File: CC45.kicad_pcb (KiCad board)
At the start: 2 copper layers, 247 x 80.8 mm, 122 parts, among them J1 AVR-ISP-6, SW1 RESET, SW10 K08, SW11 K09, SW12 K0A, SW13 K0B, SW14 K0C, SW15 K10, SW16 K11, SW17 K12, SW18 K13, SW19 K14, SW2 K00, SW20 K15, SW21 K16, SW22 K17, SW23 K18, SW24 K19, SW25 K1A, SW26 K1B, SW27 K20, SW28 K21, SW29 K22, SW3 K01, SW30 K23, SW31 K24, SW32 K25, SW33 K26, SW34 K27, SW35 K28, SW36 K29, SW37 K2A, SW38 K2B, SW39 K30, SW4 K02, SW40 K31, SW41 K32, SW42 K33, SW43 K34, SW44 K36, SW45 K38, SW46 K39, SW47 K3A, SW48 K3B, SW5 K03, SW6 K04, SW7 K05, SW8 K06, SW9 K07, U1 ATmega32U4-AU, U2 PRTR5V0U2X, X1 XTAL

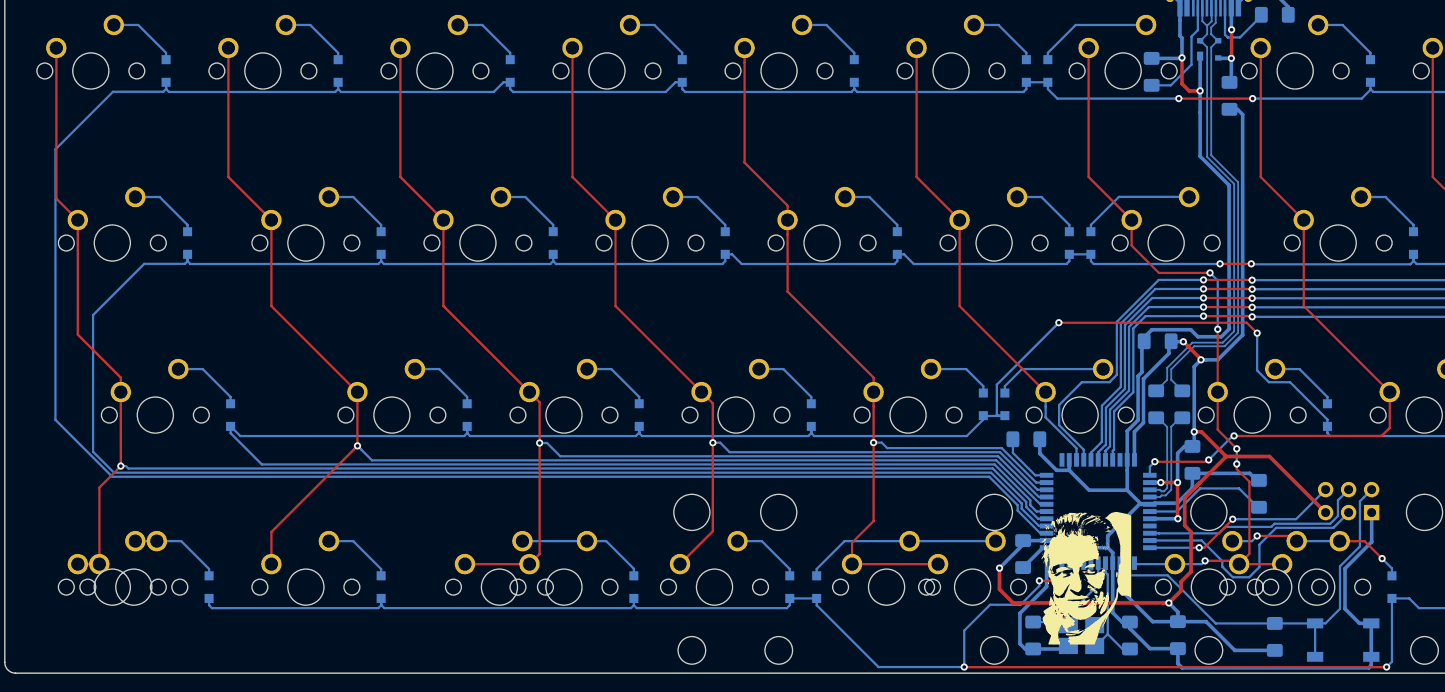
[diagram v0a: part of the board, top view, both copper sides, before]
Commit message: Add a decoupling capacitor
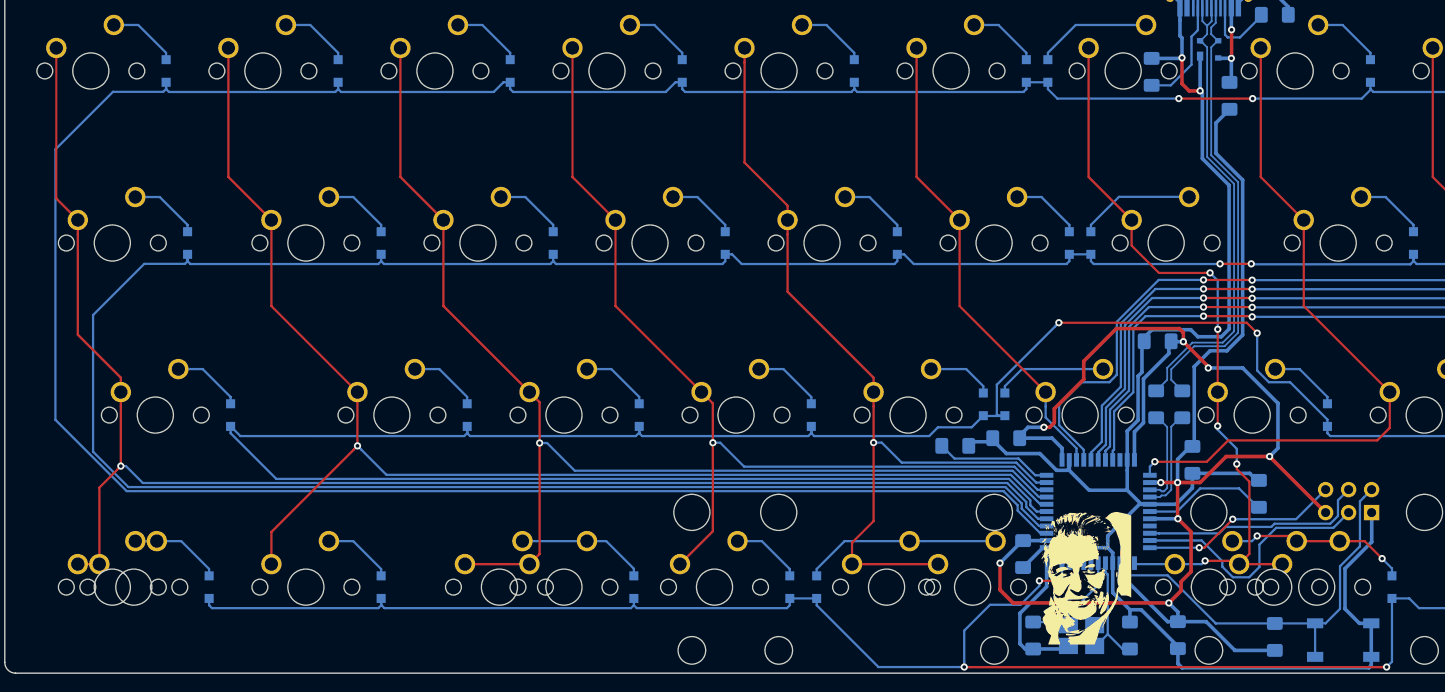
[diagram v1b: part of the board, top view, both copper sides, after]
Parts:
- added C8: 0.1u, Capacitor_SMD:C_1206_3216Metric_Pad1.42x1.75mm_HandSolder, B.Cu at (134.3, 73.8)
- SW1: value RESET -> SW_Push_Dual
- moved R1 7.88 mm to (128.7, 74.7)
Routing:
- net +5V: track 168.4 -> 210.1 mm, vias 8 -> 9
- net GND: track 231.7 -> 239.9 mm
- net Net-(R1-Pad2): track 6.26 -> 12.9 mm
- net col7: vias 3 -> 1

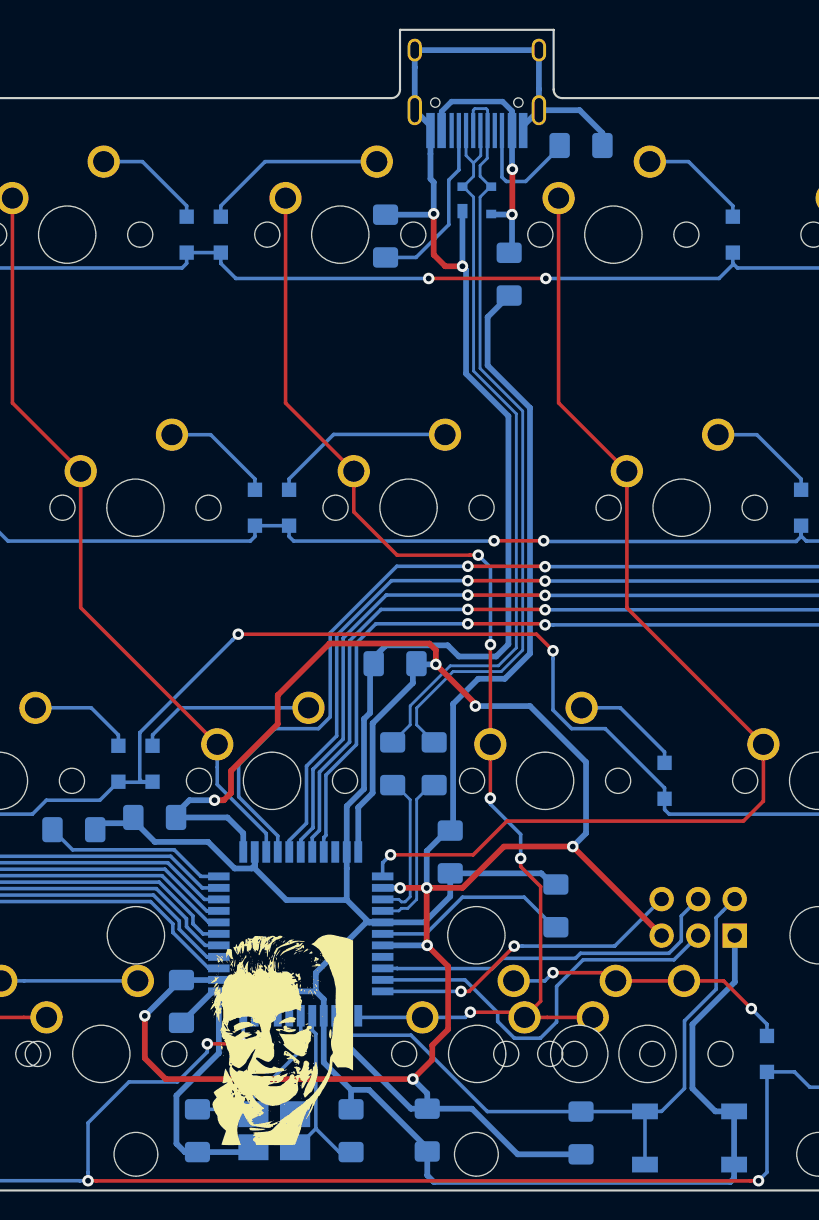
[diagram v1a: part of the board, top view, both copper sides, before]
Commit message: Add fill zones
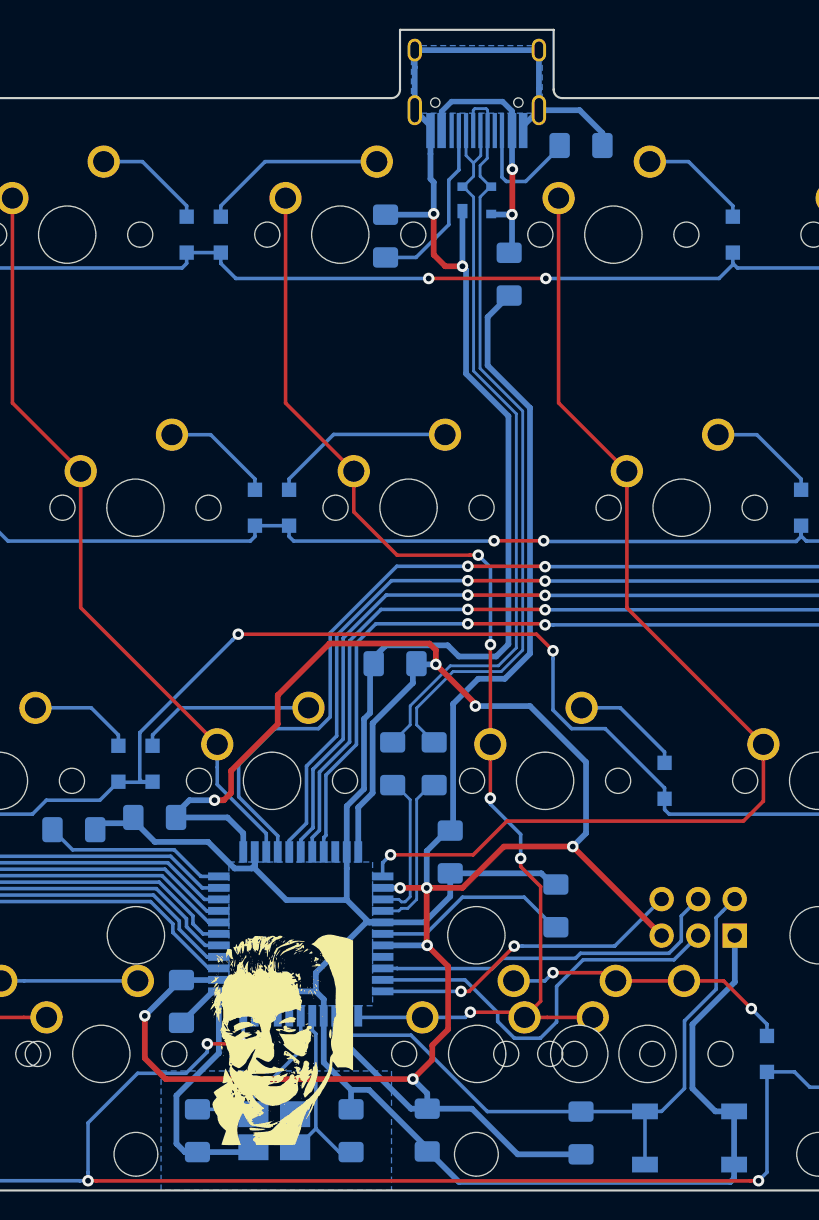
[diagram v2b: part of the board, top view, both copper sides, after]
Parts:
- SW1: value SW_Push_Dual -> RESET
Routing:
- net GND: track 239.9 -> 238.9 mm
- added copper zone on B.Cu, net GND

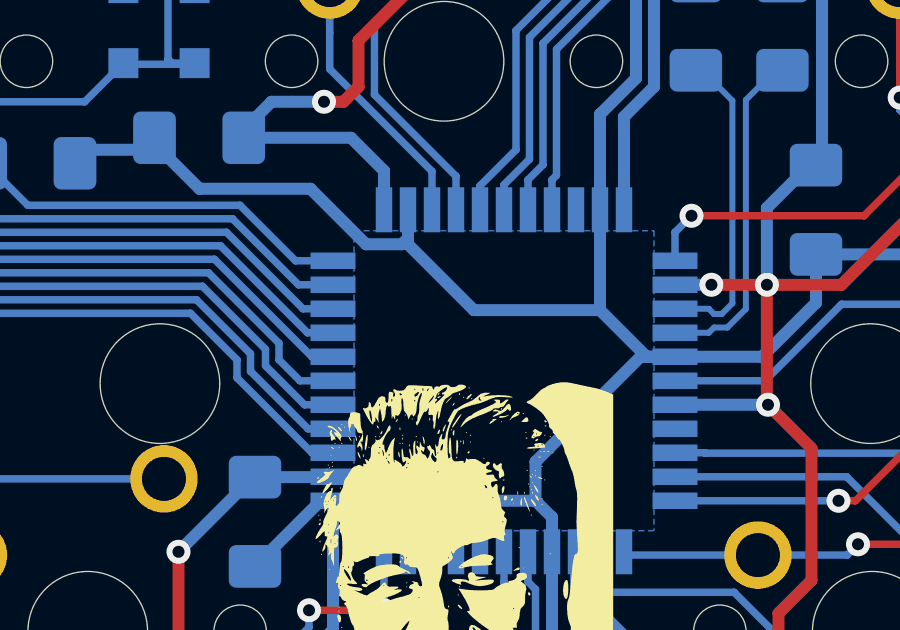
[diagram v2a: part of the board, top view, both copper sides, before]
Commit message: Visual improvements, mostly on the silkscreen
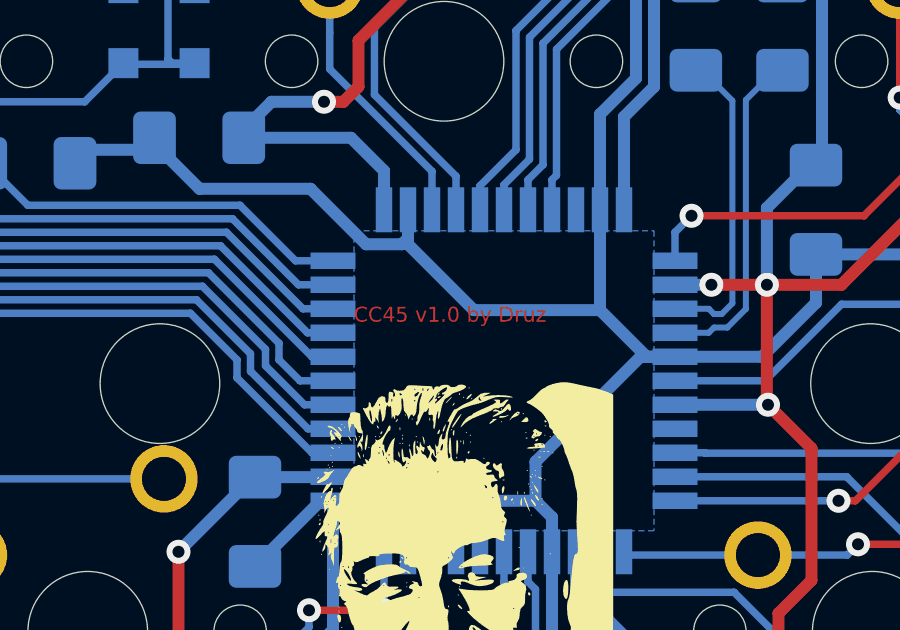
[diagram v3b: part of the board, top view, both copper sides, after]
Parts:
- C1, C2, C3, C4, C5, C6, C7, C8: footprint Capacitor_SMD:C_1206_3216Metric_Pad1.42x1.75mm_HandSolder -> custom:C_1206_3216Metric_Pad1.42x1.75mm_HandSolder
- D1, D10, D11, D12, D13, D14, D15, D16, D17, D18, D19, D2, D20, D21, D22, D23, D24, D25, D26, D27, D28, D29, D3, D30, D31, D32, D33, D34, D35, D36, D37, D38, D39, D4, D40, D41, D42, D43, D44, D45, D46, D47, D5, D6, D7, D8, D9: footprint Diode_SMD:D_SOD-323_HandSoldering -> custom:D_SOD-323_HandSoldering
- R1, R2, R3, R4, R5, R6: footprint Resistor_SMD:R_1206_3216Metric_Pad1.42x1.75mm_HandSolder -> custom:R_1206_3216Metric_Pad1.42x1.75mm_HandSolder
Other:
- board text added: "CC45 v1.0 by Druz"
- board text added: "JLCJLCJLCJLC"

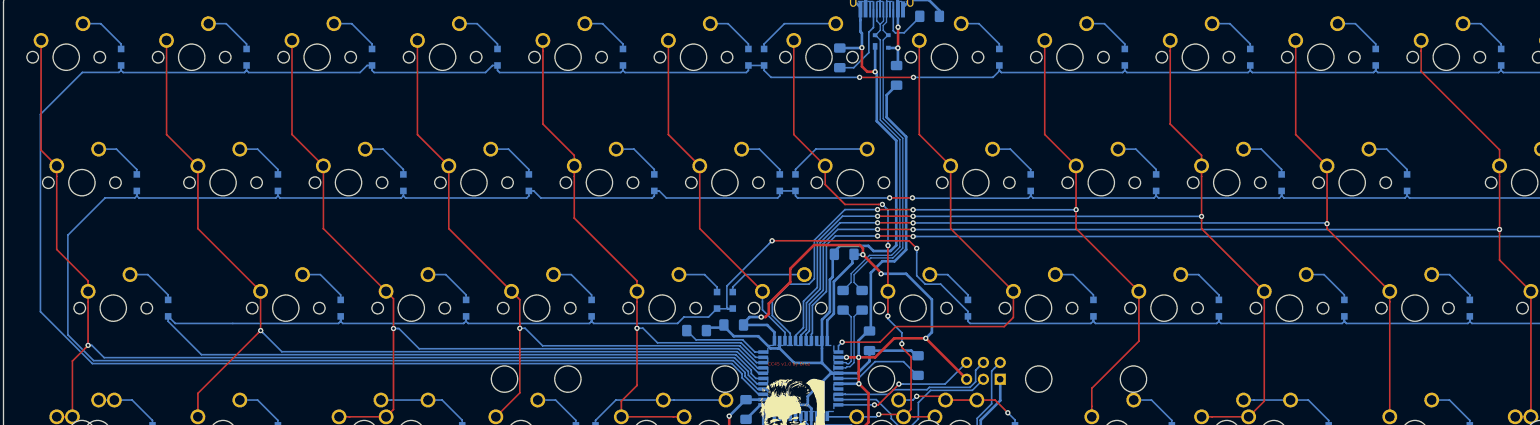
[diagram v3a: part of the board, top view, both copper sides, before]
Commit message: moving C4 closer to the mcu and adding JLC parts numbers
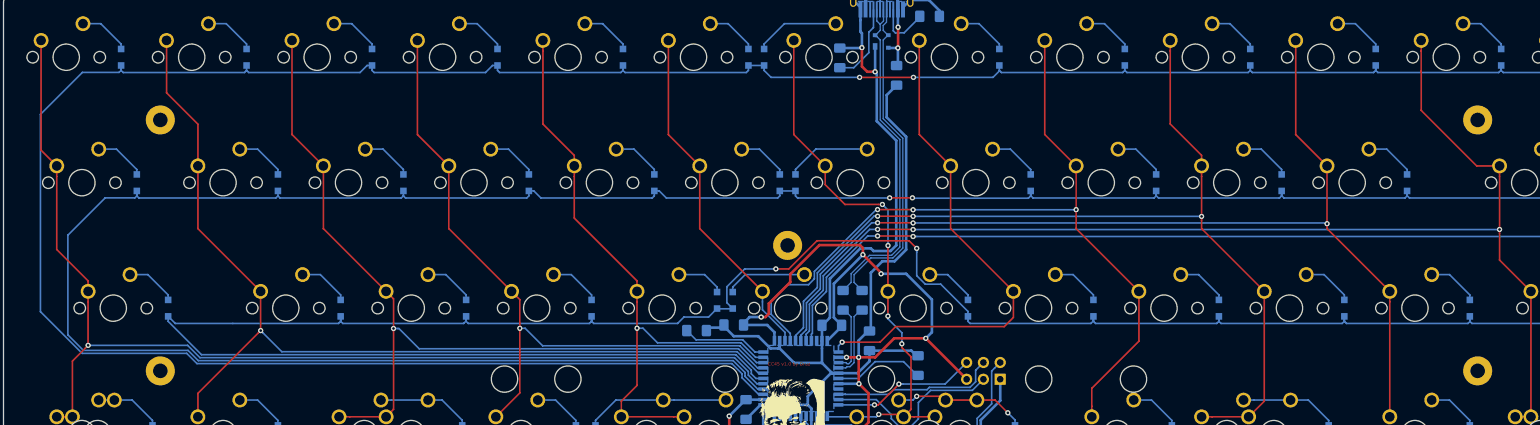
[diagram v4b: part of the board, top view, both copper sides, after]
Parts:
- added REF**: MountingHole_2.2mm_M2_Pad, MountingHole:MountingHole_2.2mm_M2_Pad, F.Cu at (142.5, 61.8)
- added REF**: MountingHole_2.2mm_M2_Pad, MountingHole:MountingHole_2.2mm_M2_Pad, F.Cu at (47.5, 42.8)
- added REF**: MountingHole_2.2mm_M2_Pad, MountingHole:MountingHole_2.2mm_M2_Pad, F.Cu at (247.0, 42.8)
- added REF**: MountingHole_2.2mm_M2_Pad, MountingHole:MountingHole_2.2mm_M2_Pad, F.Cu at (247.0, 80.8)
- added REF**: MountingHole_2.2mm_M2_Pad, MountingHole:MountingHole_2.2mm_M2_Pad, F.Cu at (47.5, 80.8)
- moved C4 10.9 mm to (149.2, 73.8)
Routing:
- net col12: track 160.6 -> 157.8 mm
- net col10: track 157.0 -> 154.2 mm
- net col9: track 147.2 -> 144.4 mm
- net col8: track 128.2 -> 125.7 mm
- net GND: track 238.9 -> 236.6 mm
- net col11: track 185.4 -> 184.6 mm
- net +5V: track 210.1 -> 209.5 mm
- net row2: track 344.2 -> 343.7 mm

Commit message: moved the middle mounting point to the center of the pcb
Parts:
- moved REF** 4.75 mm to (147.2, 61.8)
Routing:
- net +5V: track 209.5 -> 208.8 mm
